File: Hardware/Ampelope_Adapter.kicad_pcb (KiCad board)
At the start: 2 copper layers, 60.5 x 100 mm, 6 parts, among them J1 Conn_01x12_Male, J2 Conn_01x12_Male, J3 Conn_01x12_Male, J4 Conn_01x12_Male, J5 Midi_Board_Connector, J6 Filter_Connector

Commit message: Fixes to Adapter Board
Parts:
- added D1: 3d_Model_Dummy, Custom_Footprints:3D_Dummy, B.Cu at (160.5, 50.0)
- added D2: 3d_Model_Dummy, Custom_Footprints:3D_Dummy, F.Cu at (100.0, 50.0)
- J5, J6: moved to B.Cu
- moved J6 9.40 mm to (148.8, 145.7)
- moved J5 6.26 mm to (112.4, 138.2)
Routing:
- net /Audio1_In: track 83.9 -> 62.9 mm
- net /Audio4_Out: track 95.4 -> 74.7 mm
- net /Audio2_In: track 77.4 -> 62.9 mm
- net /Gate3_In: track 56.7 -> 70.1 mm
- net /Audio3_Out: track 85.6 -> 74.7 mm
- net +3V3: track 0.00 -> 7.62 mm
- net /Audio3_In: track 70.4 -> 62.9 mm
- net /Gate2_In: track 78.1 -> 72.0 mm
- net /Audio1_Out: track 64.1 -> 69.7 mm
- net /Gate4_In: track 48.6 -> 54.0 mm
- net /Audio2_Out: track 76.0 -> 74.7 mm
- net /Audio4_In: track 61.8 -> 62.9 mm
- net /Gate1_In: track 73.2 -> 73.9 mm
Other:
- outline, holes or cut-outs redrawn

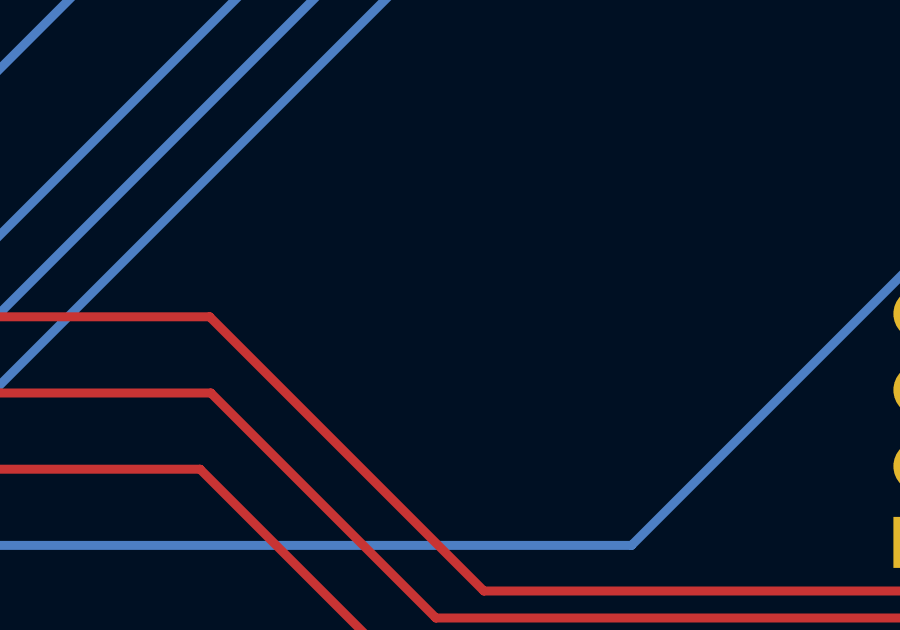
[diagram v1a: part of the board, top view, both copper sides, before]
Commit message: Added dummy connector
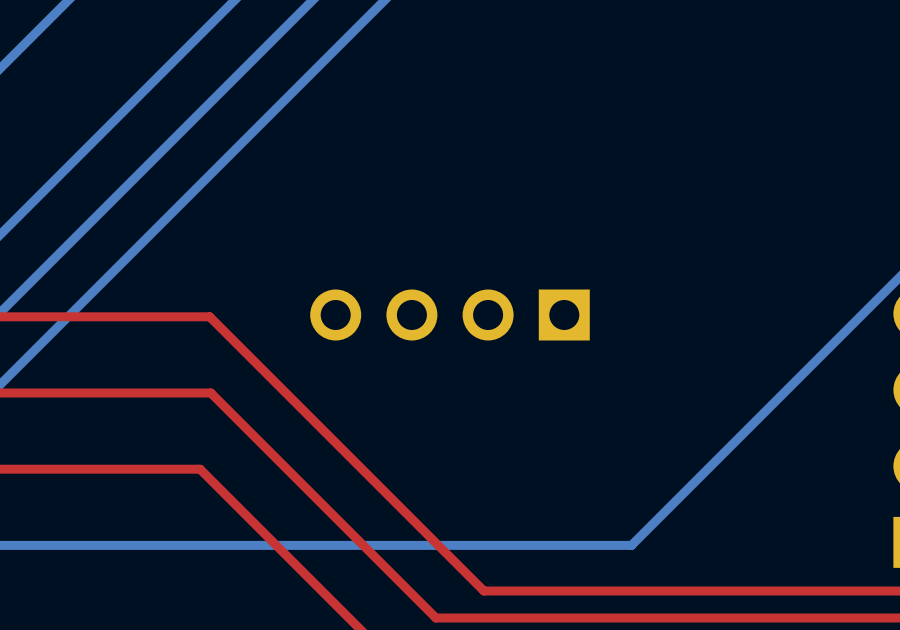
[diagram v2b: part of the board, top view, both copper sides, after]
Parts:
- added J7: Test_Connector, Connector_PinHeader_2.54mm:PinHeader_1x04_P2.54mm_Vertical, B.Cu at (137.0, 138.1)
- D1: value 3d_Model_Dummy -> 3d_Model_Components
- D2: value 3d_Model_Dummy -> 3d_Model_Controls
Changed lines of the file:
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@@
   (net 38 "/EnvB_Release")
   (net 39 "/EnvB_Sustain")
+  (net 40 "unconnected-(J7-Pad1)")
+  (net 41 "unconnected-(J7-Pad2)")
+  (net 42 "unconnected-(J7-Pad3)")
+  (net 43 "unconnected-(J7-Pad4)")
   (footprint "Custom_Footprints:3D_Dummy" (layer "F.Cu")
     (at 100 50)
@@
       (effects (font (size 1 1) (thickness 0.15)))
     )
-    (fp_text value "3d_Model_Dummy" (at 0 -3 unlocked) (layer "F.Fab")
+    (fp_text value "3d_Model_Controls" (at 0 -3 unlocked) (layer "F.Fab")
       (effects (font (size 1 1) (thickness 0.15)))
     )
@@
       (effects (font (size 1 1) (thickness 0.15)) (justify mirror))
     )
-    (fp_text value "3d_Model_Dummy" (at 0 3 unlocked) (layer "B.Fab")
+    (fp_text value "3d_Model_Components" (at 0 3 unlocked) (layer "B.Fab")
       (effects (font (size 1 1) (thickness 0.15)) (justify mirror))
     )
@@
       (offset (xyz 0 0 0))
       (scale (xyz 1 1 1))
+      (rotate (xyz 0 0 0))
+    )
+  )
+  (footprint "Connector_PinHeader_2.54mm:PinHeader_1x04_P2.54mm_Vertical" (layer "B.Cu")
+    (at 136.98 138.1 90)
+    (descr "Through hole straight pin header, 1x04, 2.54mm pitch, single row")
+    (tags "Through hole pin header THT 1x04 2.54mm single row")
+    (property "Sheetfile" "Ampelope_Adapter.kicad_sch")
+    (property "Sheetname" "")
+    (attr through_hole)
+    (fp_text reference "J7" (at 0 2.33 90) (layer "B.SilkS") hide
+      (effects (font (size 1 1) (thickness 0.15)) (justify mirror))
+    )
+    (fp_text value "Test_Connector" (at 0 -9.95 90) (layer "B.Fab")
+      (effects (font (size 1 1) (thickness 0.15)) (justify mirror))
+    )
+    (fp_text user "${REFERENCE}" (at 0 -3.81) (layer "B.Fab")
+      (effects (font (size 1 1) (thickness 0.15)) (justify mirror))
+    )
+    (fp_line (start -1.33 1.33) (end 0 1.33) (layer "B.SilkS") (width 0.12))
+    (fp_line (start -1.33 0) (end -1.33 1.33) (layer "B.SilkS") (width 0.12))
+    (fp_line (start -1.33 -8.95) (end 1.33 -8.95) (layer "B.SilkS") (width 0.12))
+    (fp_line (start -1.33 -1.27) (end 1.33 -1.27) (layer "B.SilkS") (width 0.12))
+    (fp_line (start -1.33 -1.27) (end -1.33 -8.95) (layer "B.SilkS") (width 0.12))
+    (fp_line (start 1.33 -1.27) (end 1.33 -8.95) (layer "B.SilkS") (width 0.12))
+    (fp_line (start -1.8 -9.4) (end 1.8 -9.4) (layer "B.CrtYd") (width 0.05))
+    (fp_line (start -1.8 1.8) (end -1.8 -9.4) (layer "B.CrtYd") (width 0.05))
+    (fp_line (start 1.8 1.8) (end -1.8 1.8) (layer "B.CrtYd") (width 0.05))
+    (fp_line (start 1.8 -9.4) (end 1.8 1.8) (layer "B.CrtYd") (width 0.05))
+    (fp_line (start -0.635 1.27) (end 1.27 1.27) (layer "B.Fab") (width 0.1))
+    (fp_line (start 1.27 -8.89) (end -1.27 -8.89) (layer "B.Fab") (width 0.1))
+    (fp_line (start 1.27 1.27) (end 1.27 -8.89) (layer "B.Fab") (width 0.1))
+    (fp_line (start -1.27 -8.89) (end -1.27 0.635) (layer "B.Fab") (width 0.1))
+    (fp_line (start -1.27 0.635) (end -0.635 1.27) (layer "B.Fab") (width 0.1))
+    (pad "1" thru_hole rect (at 0 0 90) (size 1.7 1.7) (drill 1) (layers *.Cu *.Mask)
+      (net 40 "unconnected-(J7-Pad1)") (pinfunction "Pin_1") (pintype "passive+no_connect"))
+    (pad "2" thru_hole oval (at 0 -2.54 90) (size 1.7 1.7) (drill 1) (layers *.Cu *.Mask)
+      (net 41 "unconnected-(J7-Pad2)") (pinfunction "Pin_2") (pintype "passive+no_connect"))
+    (pad "3" thru_hole oval (at 0 -5.08 90) (size 1.7 1.7) (drill 1) (layers *.Cu *.Mask)
+      (net 42 "unconnected-(J7-Pad3)") (pinfunction "Pin_3") (pintype "passive+no_connect"))
+    (pad "4" thru_hole oval (at 0 -7.62 90) (size 1.7 1.7) (drill 1) (layers *.Cu *.Mask)
+      (net 43 "unconnected-(J7-Pad4)") (pinfunction "Pin_4") (pintype "passive+no_connect"))
+    (model "${KICAD6_3DMODEL_DIR}/Connector_PinHeader_2.54mm.3dshapes/PinHeader_1x04_P2.54mm_Vertical.wrl"
+      (offset (xyz 0 0 0))
+      (scale (xyz 1 1 1))
